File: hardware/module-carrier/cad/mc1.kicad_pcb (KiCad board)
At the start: 2 copper layers, 160 x 100 mm, 21 parts, among them J1 FUSED ISOLATED 5V INPUT, J2 D24V22F3 external assembled b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, J3 DFR0627 WK2132 ready module h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, J4 ZAC93 ready module harness, J5 CC1101 ready module harness, J6 LD2450 radar harness, J7 BME680 external pod harness, J8 XIAO BOOT service short to GND, U1 ESP32-S3-DevKitC-1-N8R8 v1.1, U2 ESP32-H2-DevKitM-1-N4S, U3 Seeed XIAO MG24 pre-soldered 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, U4 WIZ850io finished module

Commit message: Face the RJ45 outward at the carrier edge and refresh visuals
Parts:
- moved U4 15.8 mm to (8.10, 85.0), turned to 90 degrees
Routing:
- net /+3V3: track 176.8 -> 214.4 mm, vias 1 -> 0
- net /ETH_RESET: track 65.2 -> 36.8 mm
- net /ZB_RTS: track 93.7 -> 118.1 mm, vias 0 -> 1
- net /ZB_CTS: track 144.1 -> 165.3 mm, vias 1 -> 2
- net /+5V: track 164.7 -> 185.8 mm, vias 1 -> 0
- net /ETH_MISO: track 51.7 -> 30.9 mm
- net /RADAR_RX: track 122.8 -> 102.6 mm, vias 1 -> 0
- net /RADAR_TX: track 127.3 -> 108.7 mm, vias 1 -> 0
- net /THREAD_BOOT: track 47.3 -> 61.1 mm, vias 0 -> 1
- net /ETH_MOSI: track 44.6 -> 58.4 mm, vias 0 -> 1
- net /GND: track 455.6 -> 467.8 mm, vias 0 -> 1
- net /ETH_SCK: track 42.1 -> 52.5 mm, vias 0 -> 1
- net /I2C_SCL: track 170.9 -> 163.2 mm, vias 1 -> 0
- net /ZB_TX: track 162.7 -> 169.6 mm
- net /ETH_CS: track 42.1 -> 48.3 mm, vias 0 -> 1
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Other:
- board text added: "RJ45 OUT / PLUG + LATCH CLEARANCE"

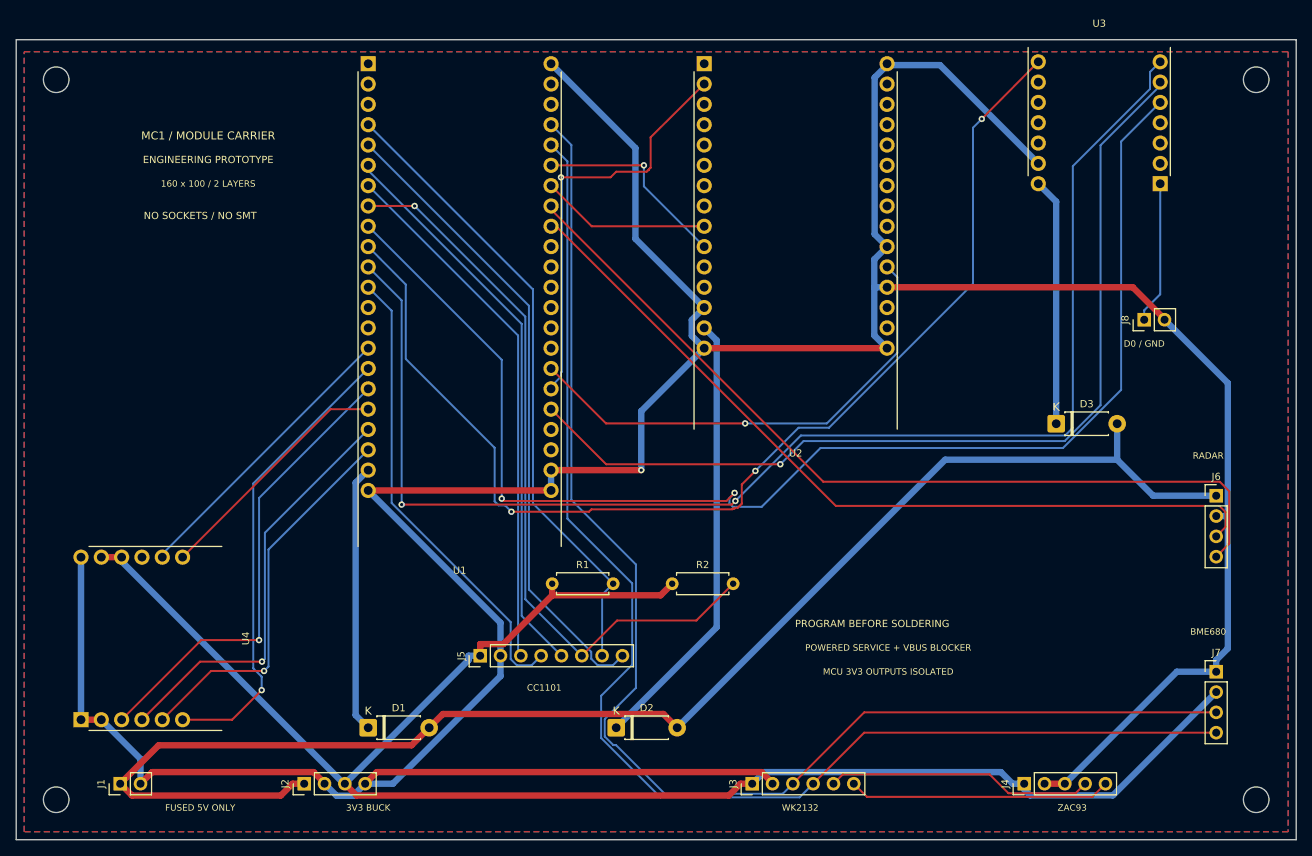
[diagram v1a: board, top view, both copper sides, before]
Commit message: Compact MC1 to 100x90 mm with accessible internal headers
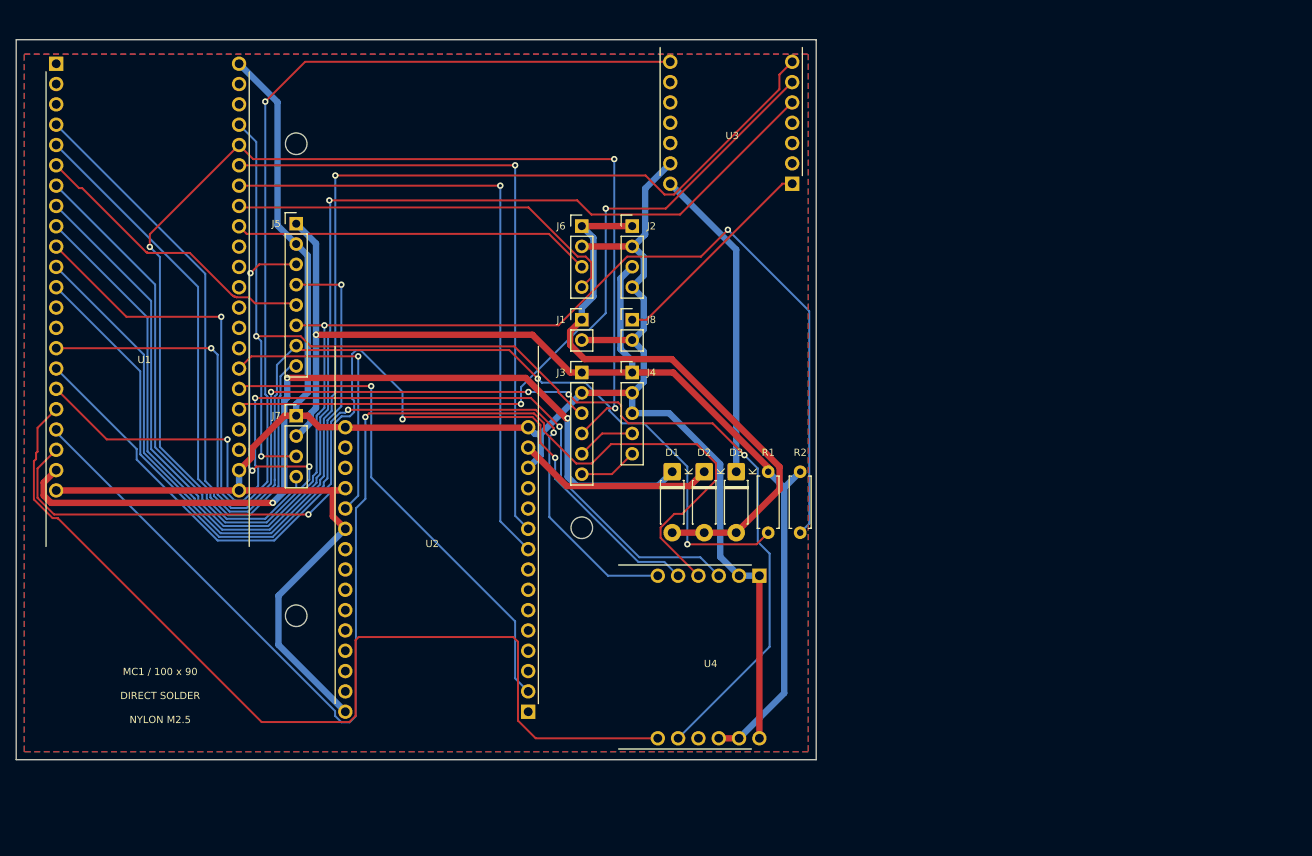
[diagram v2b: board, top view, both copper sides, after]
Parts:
- removed H4: M3 NPTH, 
- H1, H2, H3: value M3 NPTH -> M2.5 NYLON NPTH
- moved H2 137.4 mm to (35.0, 72.0)
- moved J7 119.4 mm to (35.0, 47.0)
- moved U4 86.7 mm to (92.9, 67.0), turned to -90 degrees
- moved J6 86.2 mm to (70.7, 23.3)
- moved U2 83.9 mm to (64.0, 84.0), turned to 180 degrees
- moved J1 81.8 mm to (70.7, 35.0), turned to 0 degrees
- moved J2 80.9 mm to (77.0, 23.3), turned to 0 degrees
- moved H3 74.0 mm to (70.7, 61.0)
- moved J4 71.0 mm to (77.0, 41.6), turned to 0 degrees
- moved J8 64.0 mm to (77.0, 35.0), turned to 0 degrees
- moved J5 58.7 mm to (35.0, 23.0), turned to 0 degrees
- moved J3 55.6 mm to (70.7, 41.6), turned to 0 degrees
- moved D1 49.7 mm to (82.0, 54.0), turned to -90 degrees
- moved U3 46.0 mm to (97.0, 18.0)
- moved D3 40.4 mm to (90.0, 54.0), turned to -90 degrees
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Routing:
- net /GND: track 467.8 -> 283.7 mm, vias 1 -> 0
- net /ETH_RESET: track 36.8 -> 162.7 mm, vias 0 -> 5
- net /+5V: track 185.8 -> 73.9 mm
- net /ETH_SCK: track 52.5 -> 160.0 mm
- net /ETH_MISO: track 30.9 -> 122.9 mm
- net /RF_CS: track 93.3 -> 183.7 mm, vias 1 -> 2
- net /RF_GDO0: track 79.6 -> 158.7 mm, vias 0 -> 2
- net /+5V_S3: track 33.5 -> 107.9 mm, vias 0 -> 3
- net /I2C_SDA: track 166.1 -> 91.8 mm, vias 0 -> 2
- net /ETH_CS: track 48.3 -> 122.6 mm, vias 1 -> 3
- net /+3V3: track 214.4 -> 148.9 mm, vias 0 -> 1
- net /ETH_MOSI: track 58.4 -> 117.8 mm, vias 1 -> 3
- net /THREAD_RX: track 21.2 -> 79.5 mm, vias 0 -> 1
- net /RADAR_TX: track 108.7 -> 50.6 mm
- net /RADAR_RX: track 102.6 -> 44.9 mm
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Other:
- board size 160 x 100 mm -> 100 x 90 mm
- board text added: "DIRECT SOLDER"
- board text added: "MC1 / 100 x 90"
- board text added: "NYLON M2.5"
- board text removed: "160 x 100 / 2 LAYERS"
- board text removed: "3V3 BUCK"
- board text removed: "BME680"
- board text removed: "CC1101"
- board text removed: "D0 / GND"
- board text removed: "ENGINEERING PROTOTYPE"
- board text removed: "FUSED 5V ONLY"
- board text removed: "MC1 / MODULE CARRIER"
- board text removed: "MCU 3V3 OUTPUTS ISOLATED"
- board text removed: "NO SOCKETS / NO SMT"
- board text removed: "POWERED SERVICE + VBUS BLOCKER"
- board text removed: "PROGRAM BEFORE SOLDERING"
- board text removed: "RADAR"
- board text removed: "WK2132"
- board text removed: "ZAC93"

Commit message: Implement compact Nano carrier and bounded Thread recovery
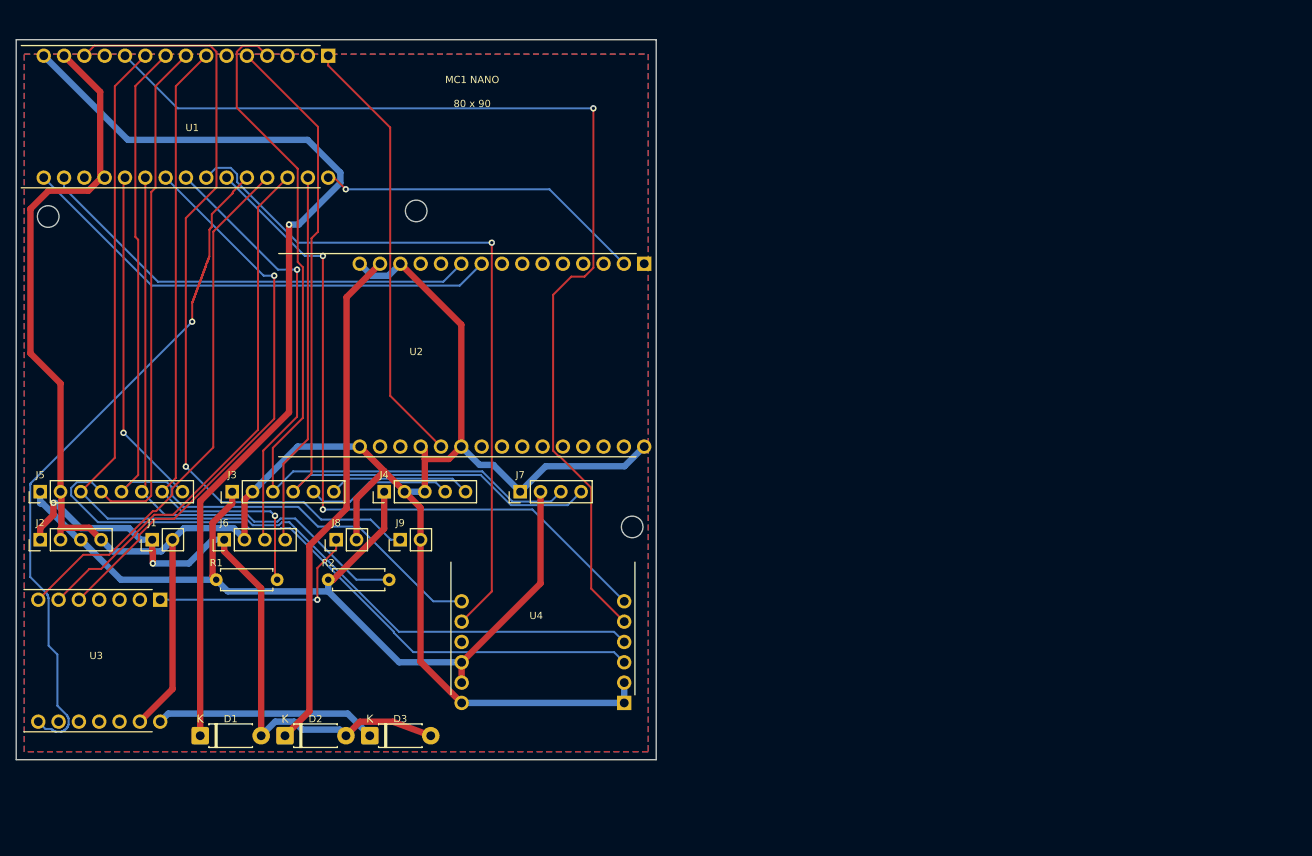
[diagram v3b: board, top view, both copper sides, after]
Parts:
- added J9: Nano GPIO0 BOOT service short to GND, MC1:PinHeader_1x02_P2.54mm_Vertical, F.Cu at (48.0, 62.5)
- U1: value ESP32-S3-DevKitC-1-N8R8 v1.1 -> Waveshare ESP32-S3-Nano-M 16MB flash 8MB PSRAM; footprint MC1:S3_DevKitC1_v11 -> MC1:S3_Nano_M
- moved U3 94.6 mm to (18.0, 70.0), turned to -90 degrees
- moved J2 83.7 mm to (3.00, 62.5), turned to 90 degrees
- moved R1 70.3 mm to (25.0, 67.5), turned to 0 degrees
- moved D1 67.6 mm to (23.0, 87.0), turned to 0 degrees
- moved D2 61.9 mm to (33.6, 87.0), turned to 0 degrees
- moved R2 60.5 mm to (39.0, 67.5), turned to 0 degrees
- moved J1 60.3 mm to (17.0, 62.5), turned to 90 degrees
- moved J6 59.5 mm to (26.0, 62.5), turned to 90 degrees
- moved U2 57.8 mm to (78.5, 28.0), turned to -90 degrees
- moved D3 56.5 mm to (44.2, 87.0), turned to 0 degrees
- moved H2 52.8 mm to (50.0, 21.4)
- moved J5 46.3 mm to (3.00, 56.5), turned to 90 degrees
- moved J3 46.2 mm to (27.0, 56.5), turned to 90 degrees
- moved J8 46.1 mm to (40.0, 62.5), turned to 90 degrees
- moved J4 34.4 mm to (46.0, 56.5), turned to 90 degrees
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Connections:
- J5 pad 3: /RF_SCK -> /SPI_SCK
- J5 pad 4: /RF_MOSI -> /SPI_MOSI
- J5 pad 5: /RF_MISO -> /SPI_MISO
- U4 pad J1.3: /ETH_MOSI -> /SPI_MOSI
- U4 pad J1.4: /ETH_SCK -> /SPI_SCK
- U4 pad J2.6: /ETH_MISO -> /SPI_MISO
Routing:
- net /ETH_SCK: track 160.0 -> 0.00 mm, vias 1 -> 0
- net /SPI_MOSI: track 0.00 -> 147.2 mm
- net /SPI_SCK: track 0.00 -> 133.9 mm
- net /ETH_MISO: track 122.9 -> 0.00 mm
- net /ETH_MOSI: track 117.8 -> 0.00 mm, vias 3 -> 0
- net /RF_CS: track 183.7 -> 75.2 mm, vias 2 -> 0
- net /SPI_MISO: track 0.00 -> 106.9 mm
- net /RF_SCK: track 103.7 -> 0.00 mm, vias 3 -> 0
- net /S3_BOOT_SERVICE: track 0.00 -> 101.4 mm, vias 0 -> 1
- net /ZB_TX: track 162.2 -> 66.8 mm, vias 1 -> 0
- net /ZB_CTS: track 161.2 -> 70.6 mm
- net /RF_MOSI: track 87.1 -> 0.00 mm, vias 1 -> 0
- net /RF_GDO0: track 158.7 -> 80.2 mm, vias 2 -> 1
- net /ETH_RESET: track 162.7 -> 89.6 mm, vias 5 -> 1
- net /ZB_RX: track 154.1 -> 86.4 mm, vias 2 -> 1
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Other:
- board size 100 x 90 mm -> 80 x 90 mm
- board text added: "80 x 90"
- board text added: "MC1 NANO"
- board text removed: "DIRECT SOLDER"
- board text removed: "MC1 / 100 x 90"
- board text removed: "NYLON M2.5"

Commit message: Compact MC1 carrier and implement network radio updates
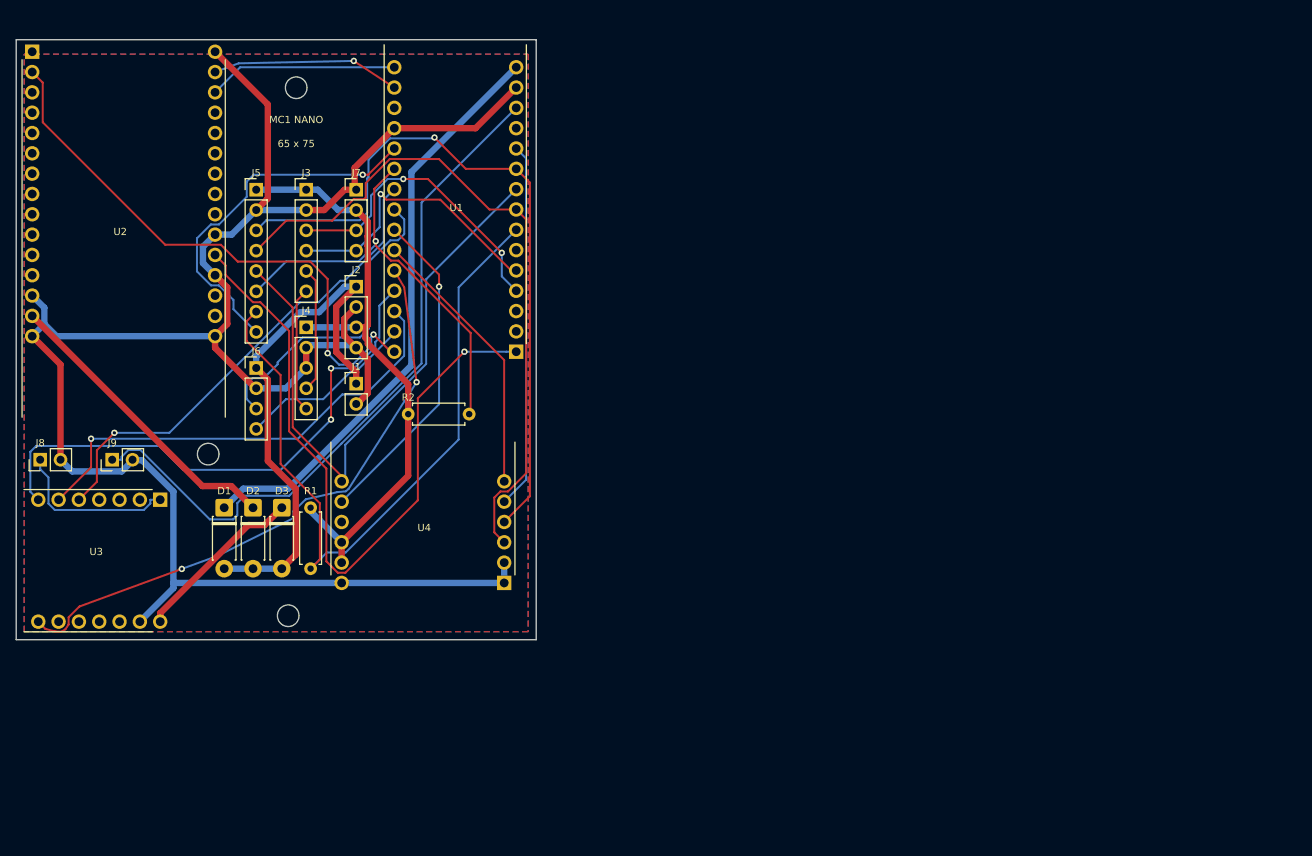
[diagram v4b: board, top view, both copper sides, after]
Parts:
- J8: value XIAO BOOT service short to GND -> XIAO BOOT unpopulated service pads
- J9: value Nano GPIO0 BOOT service short to GND -> Nano BOOT unpopulated service pads
- moved U2 81.0 mm to (2.00, 1.50), turned to 0 degrees
- moved J2 50.6 mm to (42.5, 30.9), turned to 0 degrees
- moved J5 46.4 mm to (30.0, 18.8), turned to 0 degrees
- moved H3 44.4 mm to (34.0, 72.0)
- moved U1 43.8 mm to (62.5, 39.0), turned to 180 degrees
- moved J7 43.0 mm to (42.5, 18.8), turned to 0 degrees
- moved H2 40.0 mm to (24.0, 51.8)
- moved J3 38.9 mm to (36.2, 18.8), turned to 0 degrees
- moved J8 38.3 mm to (3.00, 52.5)
- moved J9 37.4 mm to (12.0, 52.5)
- moved H1 34.9 mm to (35.0, 6.00)
- moved J1 32.1 mm to (42.5, 43.0), turned to 0 degrees
- moved D3 30.5 mm to (33.2, 58.5), turned to -90 degrees
- moved D2 28.8 mm to (29.6, 58.5), turned to -90 degrees
- moved D1 28.7 mm to (26.0, 58.5), turned to -90 degrees
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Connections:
- U2 pad J1.10: /THREAD_TX -> unconnected-(U2-GPIO5-PadJ1.10)
- U2 pad J1.9: /THREAD_RX -> unconnected-(U2-GPIO4-PadJ1.9)
- U2 pad J3.2: unconnected-(U2-GPIO24-PadJ3.2) -> /THREAD_TX
- U2 pad J3.3: unconnected-(U2-GPIO23-PadJ3.3) -> /THREAD_RX
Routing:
- net /ETH_CS: track 132.2 -> 45.8 mm, vias 1 -> 0
- net /I2C_SDA: track 103.7 -> 37.9 mm, vias 0 -> 2
- net /I2C_SCL: track 98.6 -> 35.5 mm, vias 0 -> 1
- net /SPI_MOSI: track 147.2 -> 85.8 mm
- net /ETH_INT: track 90.2 -> 34.6 mm, vias 2 -> 0
- net /ETH_RESET: track 89.6 -> 41.3 mm
- net /+5V_S3: track 121.5 -> 73.5 mm, vias 1 -> 0
- net /SPI_SCK: track 133.9 -> 88.9 mm, vias 0 -> 1
- net /+3V3: track 118.2 -> 77.4 mm
- net /GND: track 287.4 -> 249.2 mm
- net /THREAD_RX: track 61.5 -> 23.7 mm
- net /THREAD_BOOT: track 54.7 -> 87.8 mm, vias 0 -> 1
- net /THREAD_TX: track 56.7 -> 23.6 mm, vias 0 -> 1
- net /SPI_MISO: track 106.9 -> 76.3 mm
- net /THREAD_EN: track 41.4 -> 71.9 mm, vias 1 -> 2
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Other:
- board size 80 x 90 mm -> 65 x 75 mm
- board text added: "65 x 75"
- board text removed: "80 x 90"
